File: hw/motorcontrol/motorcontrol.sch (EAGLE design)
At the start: 105 parts, among them J2 USB-MICROB, U1 BTN8982TA, U10 BSS138BKS, U11 DMG2305UX, U12 BSS138BKS, U2 BTN8982TA, U3 BTN8982TA, U4 CAT24C32WI-GT3, U5 ADG3304, U6 MMDT5401, U7 PTR08060W, U8 IPD90P03P4L-04, U9 ATMEGA32U4

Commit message: list of changes for board items
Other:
- note added: "v2.1"
- note removed: "v2.0"
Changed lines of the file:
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@@
 <text x="289.56" y="22.86" size="1.9304" layer="94" align="top-left">Raspberry Pi Car Control Board
 WashU ESE Dept - May 2017</text>
-<text x="378.46" y="5.08" size="2.54" layer="94" align="bottom-center">v2.0</text>
+<text x="378.46" y="5.08" size="2.54" layer="94" align="bottom-center">v2.1</text>
 </plain>
 <instances>

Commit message: backup
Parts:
- removed C29: 10u, resistor:C-USC1206
- removed R31, R44: 3.9k, resistor:R-US_R1206
- removed U10: BSS138BKS, rpibout:BSS138BKS
- R16, R26, R27, R30, R43, R45, R46: value 3.9k -> 10k
- S1: value B3U-3000P-B -> SWITCH-GND; device rpibout:B3U-3000P-B -> rpibout:SWITCH-GND
- U5: value ADG3304 -> ADG3308; device rpibout:ADG3304 -> rpibout:ADG3308
- XTAL1: device rpibout:CRYSTAL -> rpibout:XTALABLS7M2
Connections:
- removed net D14: U9.PB0(SS)
- removed net N$48: U9.PD5(XCK/CTS)
- new net ATMEGAPD5: U5.Y8, U9.PD5(XCK/CTS)
- new net ATMEGASS: U5.Y5, U9.PB0(SS)
- new net RPICE0: J1.24, U5.A5
- net +3V3: no longer C29.1, R31.2, R44.2
- net +5V: no longer U10T1.G, U10T2.G
- net A0: now also U9.PF7(ADC7/TDI); no longer U9.PF7(ADC7(TDI)
- net ATMEGARESET: now also S1.1; no longer S1.2
- net ATMEGASCL: now also U5.Y6; no longer U10T1.S
- net ATMEGASDA: now also U5.Y7; no longer U10T2.S
- net D7: now also U9.PE6(INT6/AIN0); no longer U9.PE6(INT.6/AIN0)
- net GND: now also S1.2, S1.GND; no longer C29.2, S1.1, XTAL1.2
- net IMUSCL: now also J1.5, U5.A6; no longer R44.1, U10T1.D
- net IMUSDA: now also J1.3, U5.A7; no longer R31.1, U10T2.D
- net N$3: now also XTAL1.2; no longer XTAL1.3
- net RPILEDB: now also J1.10, U5.A8; no longer J1.5
- net RPILEDG: now also J1.12; no longer J1.3
- net RPIRESET: now also J1.22; no longer J1.12
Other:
- moved on the sheet: C23, C24, C38, R30, R43

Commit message: backup
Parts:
- D1: device diode:ZENER-DIODESOD80C -> rpibout:ZENER_DIODESOD123
- D2: device rpibout:SMAZX -> rpibout:ZENER_DIODESMA
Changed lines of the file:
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@@
 <part name="R14" library="resistor" deviceset="R-US_" device="R1206" value="10k"/>
 <part name="GND17" library="supply1" deviceset="GND" device=""/>
-<part name="D1" library="diode" deviceset="ZENER-DIODE" device="SOD80C" value="10V"/>
 <part name="C17" library="resistor" deviceset="C-US" device="C1206" value="0.1u"/>
 <part name="GND18" library="supply1" deviceset="GND" device=""/>
@@
 <part name="U7" library="rpibout" deviceset="PTR08060W" device=""/>
 <part name="C16" library="resistor" deviceset="CPOL-US" device="E5-10.5" value="1000u"/>
-<part name="D2" library="rpibout" deviceset="SMAZX" device="" value="33V"/>
 <part name="R16" library="resistor" deviceset="R-US_" device="R1206" value="10k"/>
 <part name="P+5" library="supply1" deviceset="+5V" device=""/>
@@
 <part name="XTAL1" library="rpibout" deviceset="XTAL" device="ABLS7M2" value="16MHz"/>
 <part name="S1" library="rpibout" deviceset="SWITCH-GND" device=""/>
+<part name="D1" library="rpibout" deviceset="ZENER_DIODE" device="SOD123" value="10V"/>
+<part name="D2" library="rpibout" deviceset="ZENER_DIODE" device="SMA" value="33V"/>
 </parts>
 <sheets>
@@
 </instance>
 <instance part="GND17" gate="1" x="60.96" y="12.7"/>
-<instance part="D1" gate="G$1" x="60.96" y="35.56" rot="R90"/>
 <instance part="C17" gate="G$1" x="33.02" y="35.56"/>
 <instance part="GND18" gate="1" x="33.02" y="25.4"/>
@@
 <instance part="U7" gate="G$1" x="63.5" y="83.82"/>
 <instance part="C16" gate="G$1" x="81.28" y="35.56"/>
-<instance part="D2" gate="G$1" x="71.12" y="33.02" rot="R90"/>
 <instance part="R16" gate="G$1" x="210.82" y="213.36" smashed="yes" rot="R90">
 <attribute name="NAME" x="212.1154" y="216.154" size="1.778" layer="95"/>
@@
 <instance part="XTAL1" gate="G$1" x="129.54" y="175.26" rot="R270"/>
 <instance part="S1" gate="G$1" x="121.92" y="218.44" rot="R270"/>
+<instance part="D1" gate="G$1" x="60.96" y="35.56" rot="R90"/>
+<instance part="D2" gate="G$1" x="71.12" y="33.02" rot="R90"/>
 </instances>
 <busses>
@@
 <wire x1="60.96" y1="27.94" x2="60.96" y2="30.48" width="0.1524" layer="91"/>
 <pinref part="R14" gate="G$1" pin="2"/>
-<pinref part="D1" gate="G$1" pin="A"/>
 <wire x1="60.96" y1="30.48" x2="53.34" y2="30.48" width="0.1524" layer="91"/>
 <wire x1="53.34" y1="30.48" x2="53.34" y2="35.56" width="0.1524" layer="91"/>
@@
 <junction x="60.96" y="30.48"/>
 <pinref part="U8" gate="G$1" pin="G"/>
+<pinref part="D1" gate="G$1" pin="A"/>
 </segment>
 </net>
@@
 <net name="VPP" class="0">
 <segment>
-<pinref part="D1" gate="G$1" pin="C"/>
 <wire x1="55.88" y1="40.64" x2="60.96" y2="40.64" width="0.1524" layer="91"/>
 <wire x1="60.96" y1="40.64" x2="71.12" y2="40.64" width="0.1524" layer="91"/>
@@
 <pinref part="U8" gate="G$1" pin="S"/>
 <pinref part="C16" gate="G$1" pin="+"/>
+<pinref part="D1" gate="G$1" pin="C"/>
 <pinref part="D2" gate="G$1" pin="C"/>
 </segment>

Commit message: backup
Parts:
- LED1: value MSL0201RGB -> LED_3COLOR_COMMONA1411; device rpibout:MSL0201RGB -> rpibout:LED_3COLOR_COMMONA1411
- R15: value 0.51k -> 267
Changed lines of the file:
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@@
 <part name="P+6" library="supply1" deviceset="+5V" device=""/>
 <part name="GND27" library="supply1" deviceset="GND" device=""/>
-<part name="R15" library="resistor" deviceset="R-US_" device="R1206" value="0.51k"/>
+<part name="R15" library="resistor" deviceset="R-US_" device="R1206" value="267"/>
 <part name="U6" library="rpibout" deviceset="MMDT5401" device=""/>
 <part name="U4" library="rpibout" deviceset="CAT24C32WI-GT3" device=""/>
@@
 <part name="P+5" library="supply1" deviceset="+5V" device=""/>
 <part name="S2" library="rpibout" deviceset="A6HF-2DIP" device=""/>
-<part name="LED1" library="rpibout" deviceset="MSL0201RGB" device=""/>
 <part name="+3V5" library="supply1" deviceset="+3V3" device=""/>
 <part name="U12" library="rpibout" deviceset="BSS138BKS" device=""/>
@@
 <part name="D1" library="rpibout" deviceset="ZENER_DIODE" device="SOD123" value="10V"/>
 <part name="D2" library="rpibout" deviceset="ZENER_DIODE" device="SMA" value="33V"/>
+<part name="LED1" library="rpibout" deviceset="LED_3COLOR_COMMONA" device="1411"/>
 </parts>
 <sheets>
@@
 <instance part="S2" gate="P1" x="25.4" y="218.44"/>
 <instance part="S2" gate="P2" x="218.44" y="208.28"/>
-<instance part="LED1" gate="G$1" x="81.28" y="127"/>
 <instance part="+3V5" gate="G$1" x="78.74" y="152.4"/>
 <instance part="U12" gate="T1" x="86.36" y="119.38"/>
@@
 <instance part="D1" gate="G$1" x="60.96" y="35.56" rot="R90"/>
 <instance part="D2" gate="G$1" x="71.12" y="33.02" rot="R90"/>
+<instance part="LED1" gate="G$1" x="81.28" y="127"/>
 </instances>
 <busses>
@@
 <segment>
 <pinref part="GND27" gate="1" pin="GND"/>
-<pinref part="LED1" gate="G$1" pin="R"/>
 <wire x1="86.36" y1="127" x2="93.98" y2="127" width="0.1524" layer="91"/>
 <wire x1="93.98" y1="127" x2="93.98" y2="114.3" width="0.1524" layer="91"/>
@@
 <pinref part="U12" gate="T2" pin="S"/>
 <wire x1="93.98" y1="114.3" x2="111.76" y2="114.3" width="0.1524" layer="91"/>
+<pinref part="LED1" gate="G$1" pin="R"/>
 </segment>
 <segment>
@@
 <segment>
 <pinref part="R15" gate="G$1" pin="1"/>
+<wire x1="78.74" y1="137.16" x2="78.74" y2="134.62" width="0.1524" layer="91"/>
 <pinref part="LED1" gate="G$1" pin="A"/>
-<wire x1="78.74" y1="137.16" x2="78.74" y2="134.62" width="0.1524" layer="91"/>
 </segment>
 </net>
 <net name="N$14" class="0">
 <segment>
-<pinref part="LED1" gate="G$1" pin="B"/>
 <pinref part="U12" gate="T1" pin="D"/>
 <wire x1="86.36" y1="124.46" x2="88.9" y2="124.46" width="0.1524" layer="91"/>
+<pinref part="LED1" gate="G$1" pin="B"/>
 </segment>
 </net>
 <net name="N$22" class="0">
 <segment>
-<pinref part="LED1" gate="G$1" pin="G"/>
 <pinref part="U12" gate="T2" pin="D"/>
 <wire x1="86.36" y1="129.54" x2="111.76" y2="129.54" width="0.1524" layer="91"/>
 <wire x1="111.76" y1="129.54" x2="111.76" y2="124.46" width="0.1524" layer="91"/>
-</segment>
-</net>
+<pinref part="LED1" gate="G$1" pin="G"/>
+</segment>
+</net>

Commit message: new schematic is ready
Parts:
- removed C22: 0.1u, resistor:C-USC1206
- added R19, R20, R21, R22, R23: 10k, resistor:R-US_R1206
- added U10: SN74LV4T125, rpibout:SN74LV4T125
- added U13: BSS138BKS, rpibout:BSS138BKS
- U5: value ADG3308 -> SN74LV4T125; device rpibout:ADG3308 -> rpibout:SN74LV4T125
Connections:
- net N$23 renamed ATMEGAD-
- net N$24 renamed ATMEGAD+
- new net RPIGND: J1.25, R22.1, U5G1.OE, U5G2.OE, U5G3.OE, U5G4.OE
- net +3V3: now also R20.2, R21.2, R48.2, U10PWR.VCC, U13T1.G, U13T2.G; no longer S2P1.1, U5.VCCA
- net +5V: now also R19.2, R22.2, R23.2, U5PWR.VCC; no longer C22.1, R48.2, U5.EN, U5.VCCY
- net ATMEGAMISO: now also U10G1.I; no longer U5.Y2
- net ATMEGAMOSI: now also U5G1.O; no longer U5.Y1
- net ATMEGAPD5: now also U10G2.I; no longer U5.Y8
- net ATMEGARESET: now also R23.1, U5G3.O; no longer C22.2, R48.1, S1.1, U5.Y4
- net ATMEGASCK: now also U5G2.O; no longer U5.Y3
- net ATMEGASCL: now also U13T1.D; no longer U5.Y6
- net ATMEGASDA: now also U13T2.D; no longer U5.Y7
- net ATMEGASS: now also U5G4.O; no longer U5.Y5
- net GND: now also U10G1.OE, U10G2.OE, U10G3.I, U10G3.OE, U10G4.I, U10G4.OE, U10PWR.GND, U5PWR.GND; no longer J1.25, U5.GND
- net IMUSCL: now also R20.1, U13T1.S; no longer U5.A6
- net IMUSDA: now also R21.1, U13T2.S; no longer U5.A7
- net N$12: now also R19.1; no longer S2P1.2, U4.WP
- net RPICE0: now also U5G4.I; no longer U5.A5
- net RPILEDB: now also U10G2.O; no longer U5.A8
- net RPIMISO: now also U10G1.O; no longer U5.A2
- net RPIMOSI: now also U5G1.I; no longer U5.A1
- net RPIRESET: now also R48.1, S1.1, U5G3.I; no longer U5.A4
- net RPISCK: now also U5G2.I; no longer U5.A3
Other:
- moved on the sheet: C1, C10, C11, C12, C13, C14, C15, C2, C23, C24, C27, C28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

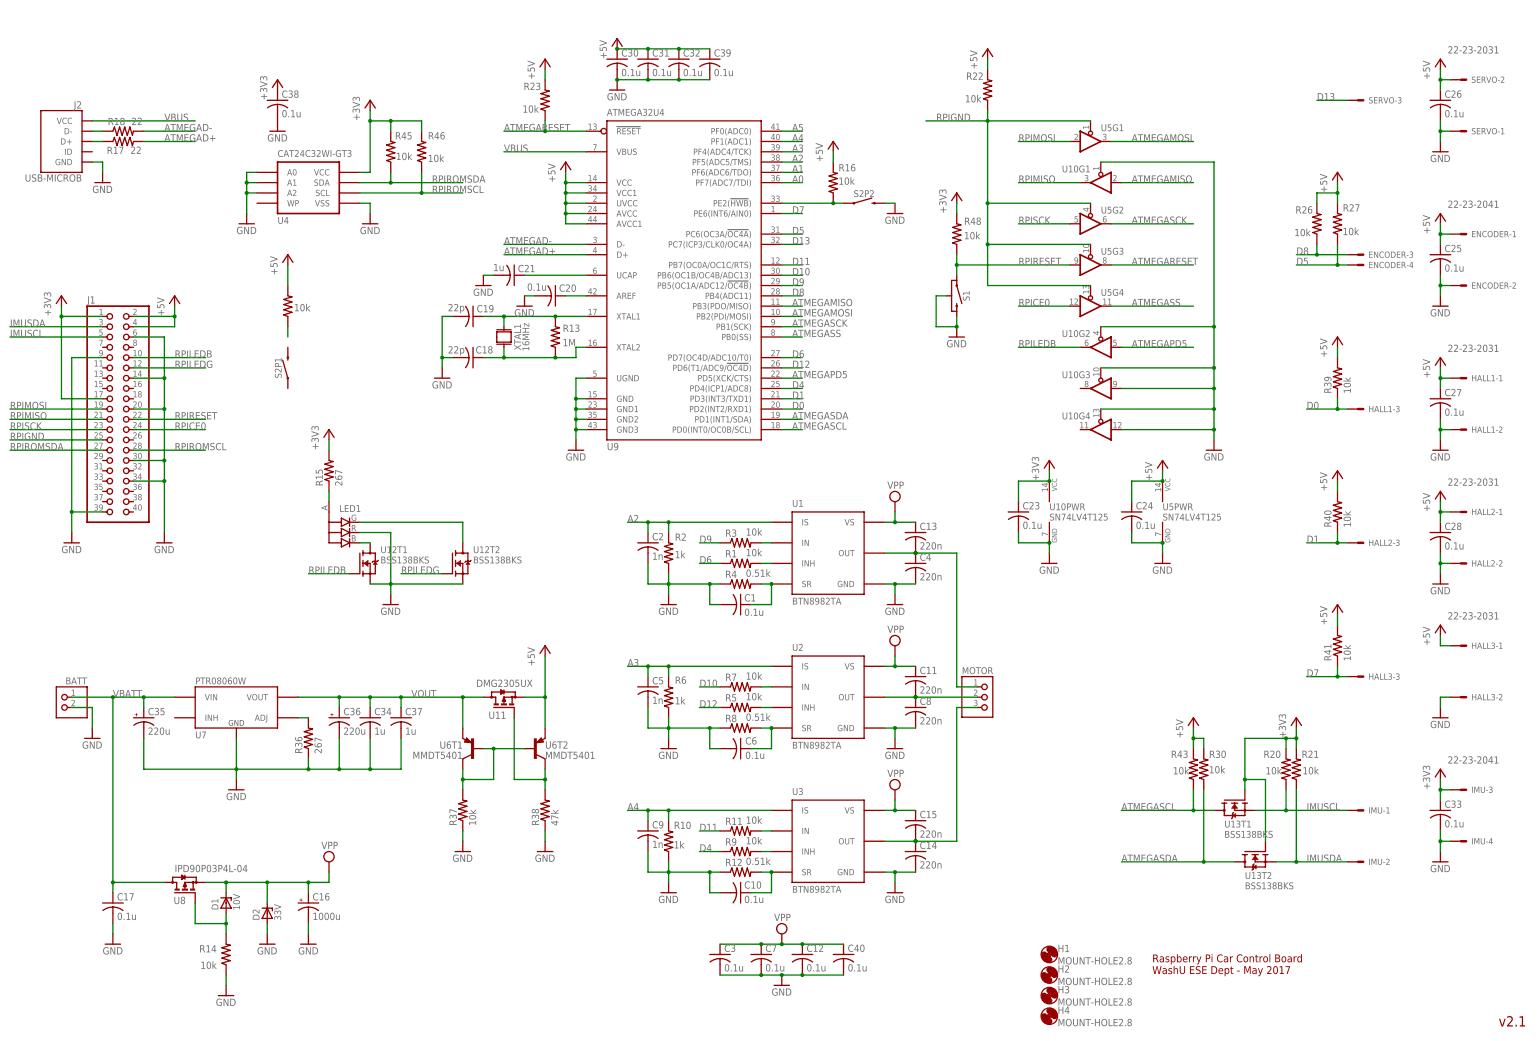
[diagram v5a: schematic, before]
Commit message: fixed RPi-Arduino buffer for reset pin
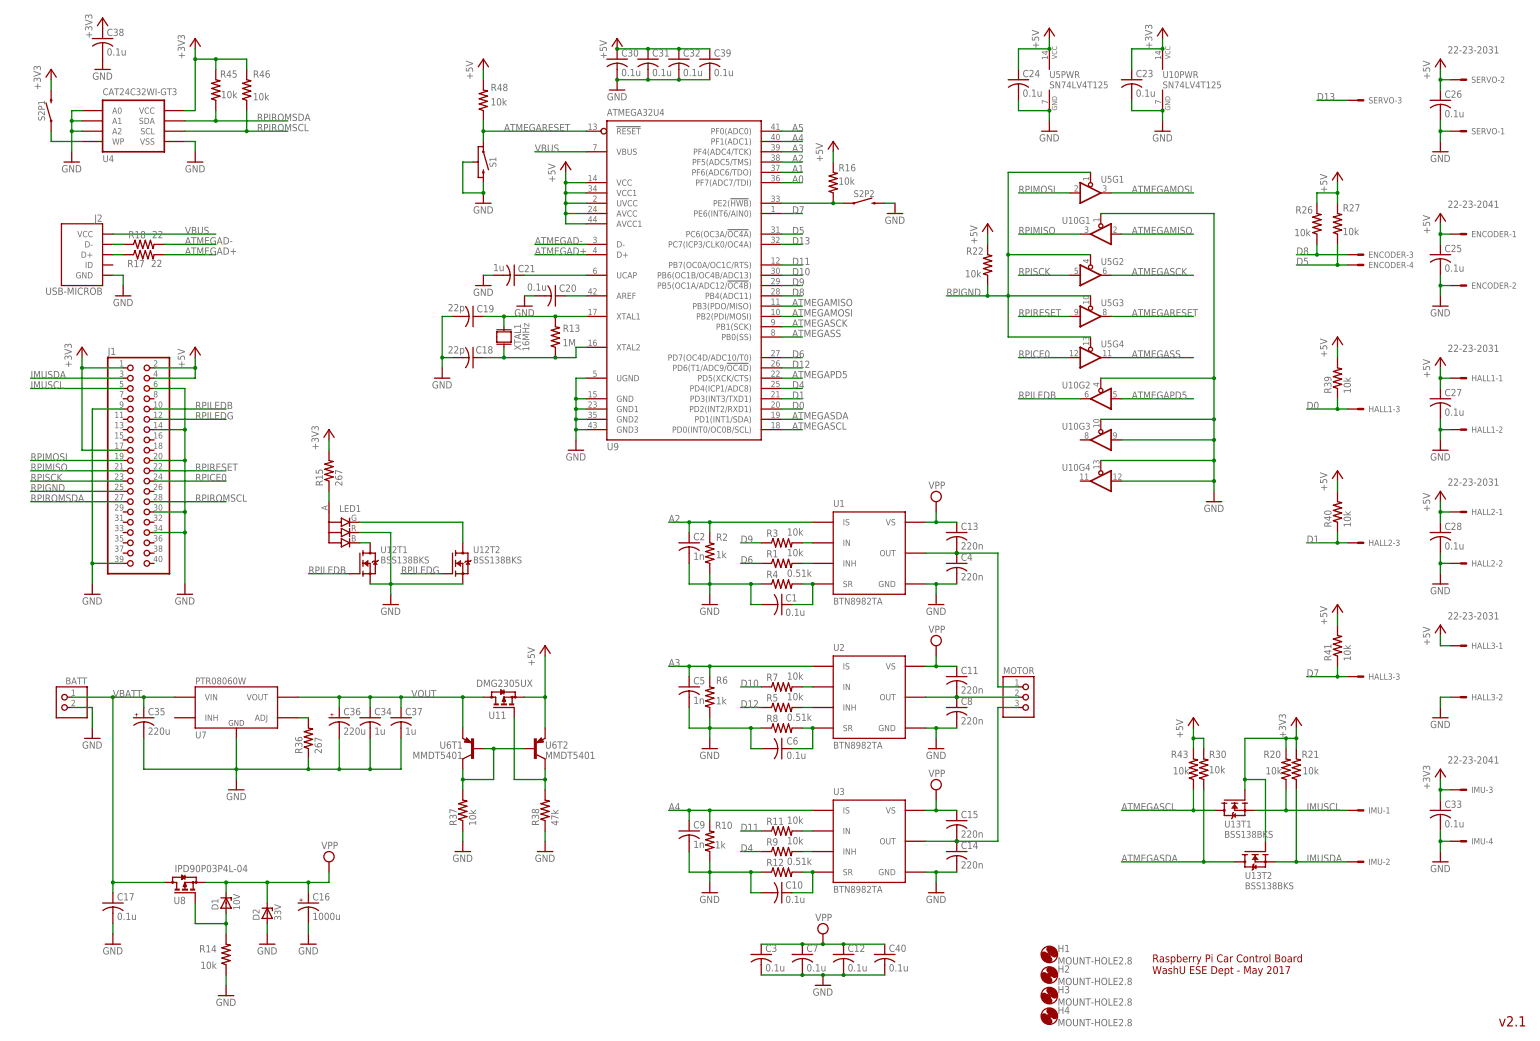
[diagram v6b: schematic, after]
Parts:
- removed R19, R23: 10k, resistor:R-US_R1206
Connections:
- net +3V3: now also S2P1.2; no longer R48.2
- net +5V: now also R48.2; no longer R19.2, R23.2
- net ATMEGARESET: now also R48.1, S1.1; no longer R23.1
- net N$12: now also S2P1.1, U4.WP; no longer R19.1
- net RPIRESET: no longer R48.1, S1.1
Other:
- moved on the sheet: C1, C10, C11, C12, C13, C14, C15, C2, C23, C24, C3, C38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

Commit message: backup
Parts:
- removed C37: 1u, resistor:C-USC1206
- U11: value DMG2305UX -> SI2333CDS-T1-GE3; device rpibout:DMG2305UX -> rpibout:SI2333CDS-T1-GE3
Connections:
- net GND: no longer C37.2
- net VOUT: no longer C37.1
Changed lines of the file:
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@@
 <part name="BATT" library="rpibout" deviceset="ULTRAFIT_2CIRC" device="VCLIP"/>
 <part name="GND45" library="supply1" deviceset="GND" device=""/>
-<part name="C37" library="resistor" deviceset="C-US" device="C1206" value="1u"/>
 <part name="R37" library="resistor" deviceset="R-US_" device="R1206" value="10k"/>
 <part name="R38" library="resistor" deviceset="R-US_" device="R1206" value="47k"/>
@@
 <part name="GND47" library="supply1" deviceset="GND" device=""/>
 <part name="P+9" library="supply1" deviceset="+5V" device=""/>
-<part name="U11" library="rpibout" deviceset="DMG2305UX" device=""/>
 <part name="HALL1" library="con-molex" deviceset="22-23-2031" device=""/>
 <part name="HALL2" library="con-molex" deviceset="22-23-2031" device=""/>
@@
 <part name="P+8" library="supply1" deviceset="+5V" device=""/>
 <part name="+3V6" library="supply1" deviceset="+3V3" device=""/>
+<part name="U11" library="rpibout" deviceset="SI2333CDS-T1-GE3" device=""/>
 </parts>
 <sheets>
@@
 <instance part="BATT" gate="G$1" x="20.32" y="86.36" rot="MR0"/>
 <instance part="GND45" gate="1" x="27.94" y="76.2"/>
-<instance part="C37" gate="G$1" x="104.14" y="81.28"/>
 <instance part="R37" gate="G$1" x="119.38" y="58.42" rot="R90"/>
 <instance part="R38" gate="G$1" x="139.7" y="58.42" rot="R90"/>
@@
 <instance part="GND47" gate="1" x="139.7" y="48.26"/>
 <instance part="P+9" gate="1" x="139.7" y="99.06"/>
-<instance part="U11" gate="G$1" x="129.54" y="86.36" smashed="yes" rot="MR90">
-<attribute name="NAME" x="125.73" y="82.804" size="1.778" layer="95" rot="MR180"/>
-<attribute name="VALUE" x="122.682" y="90.678" size="1.778" layer="96" rot="MR180"/>
-</instance>
 <instance part="HALL1" gate="-1" x="365.76" y="165.1" smashed="yes">
 <attribute name="NAME" x="368.3" y="164.338" size="1.524" layer="95"/>
@@
 <instance part="P+8" gate="1" x="124.46" y="243.84"/>
 <instance part="+3V6" gate="G$1" x="17.78" y="241.3"/>
+<instance part="U11" gate="G$1" x="129.54" y="86.36" rot="MR90"/>
 </instances>
 <busses>
@@
 <pinref part="C35" gate="G$1" pin="-"/>
 <pinref part="C36" gate="G$1" pin="-"/>
-<pinref part="C37" gate="G$1" pin="2"/>
-<wire x1="96.52" y1="68.58" x2="104.14" y2="68.58" width="0.1524" layer="91"/>
-<wire x1="104.14" y1="68.58" x2="104.14" y2="76.2" width="0.1524" layer="91"/>
-<junction x="96.52" y="68.58"/>
 <pinref part="U7" gate="G$1" pin="GND"/>
 </segment>
@@
 </segment>
 <segment>
-<pinref part="U11" gate="G$1" pin="S"/>
 <wire x1="134.62" y1="86.36" x2="139.7" y2="86.36" width="0.1524" layer="91"/>
 <pinref part="P+9" gate="1" pin="+5V"/>
@@
 <wire x1="139.7" y1="78.74" x2="139.7" y2="86.36" width="0.1524" layer="91"/>
 <junction x="139.7" y="86.36"/>
+<pinref part="U11" gate="G$1" pin="S"/>
 </segment>
 <segment>
@@
 <wire x1="96.52" y1="86.36" x2="88.9" y2="86.36" width="0.1524" layer="91"/>
 <pinref part="C36" gate="G$1" pin="+"/>
-<pinref part="C37" gate="G$1" pin="1"/>
-<wire x1="96.52" y1="86.36" x2="104.14" y2="86.36" width="0.1524" layer="91"/>
-<wire x1="104.14" y1="86.36" x2="104.14" y2="83.82" width="0.1524" layer="91"/>
 <junction x="96.52" y="86.36"/>
-<pinref part="U11" gate="G$1" pin="D"/>
 <wire x1="124.46" y1="86.36" x2="119.38" y2="86.36" width="0.1524" layer="91"/>
-<junction x="104.14" y="86.36"/>
 <pinref part="U6" gate="T1" pin="E"/>
-<wire x1="119.38" y1="86.36" x2="104.14" y2="86.36" width="0.1524" layer="91"/>
+<wire x1="119.38" y1="86.36" x2="96.52" y2="86.36" width="0.1524" layer="91"/>
 <wire x1="119.38" y1="78.74" x2="119.38" y2="86.36" width="0.1524" layer="91"/>
 <junction x="119.38" y="86.36"/>
 <pinref part="U7" gate="G$1" pin="VOUT"/>
 <label x="106.68" y="86.36" size="1.778" layer="95"/>
+<pinref part="U11" gate="G$1" pin="D"/>
 </segment>
 </net>
@@
 <net name="N$2" class="0">
 <segment>
-<pinref part="U11" gate="G$1" pin="G"/>
 <wire x1="132.08" y1="81.28" x2="132.08" y2="66.04" width="0.1524" layer="91"/>
 <wire x1="132.08" y1="66.04" x2="139.7" y2="66.04" width="0.1524" layer="91"/>
@@
 <wire x1="139.7" y1="63.5" x2="139.7" y2="66.04" width="0.1524" layer="91"/>
 <junction x="139.7" y="66.04"/>
-</segment>
-</net>
+<pinref part="U11" gate="G$1" pin="G"/>
+</segment>
+</net>
